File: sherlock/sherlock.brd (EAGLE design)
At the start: 91.4 x 58.4 mm, 27 parts, among them U3 XBEE-1B2, X1 2540-

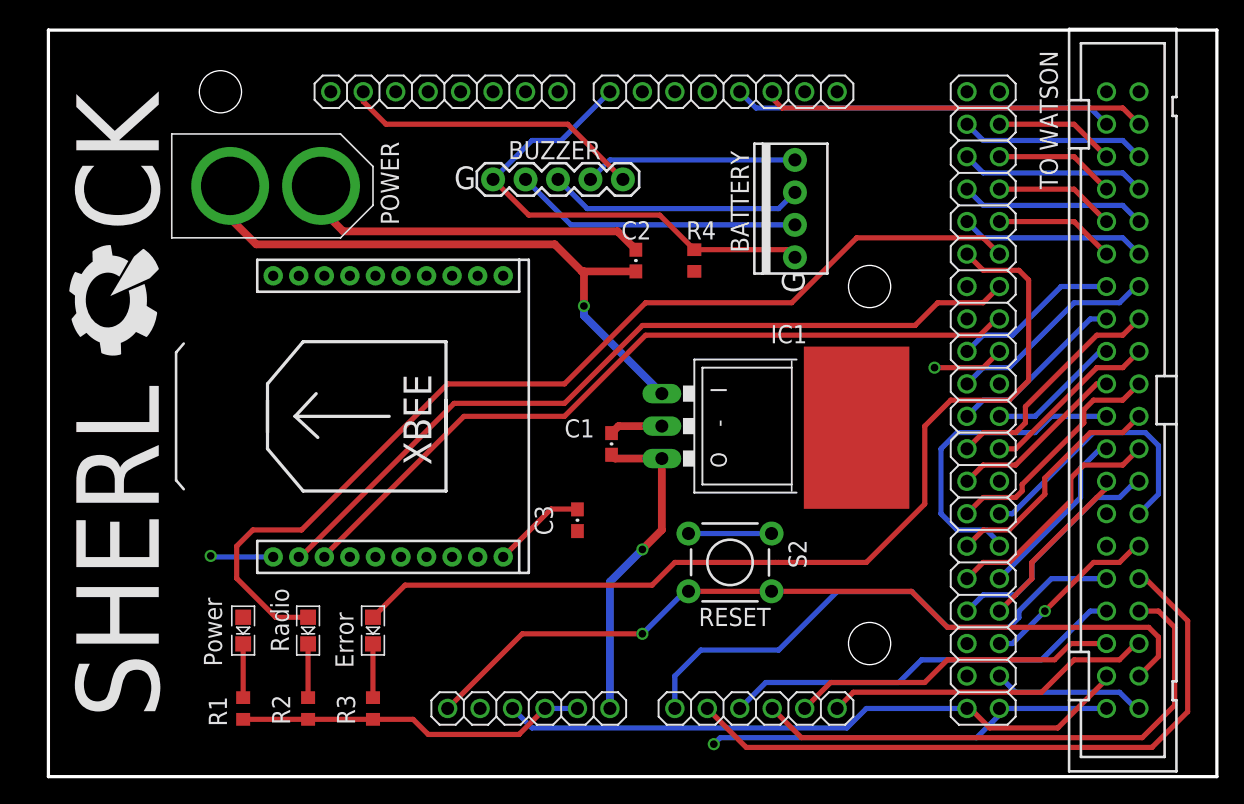
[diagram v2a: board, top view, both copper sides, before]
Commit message: Added Andersons
Also deleted sherlock_anderson because it's outdated and redundant (uses
last year's Sherlock).
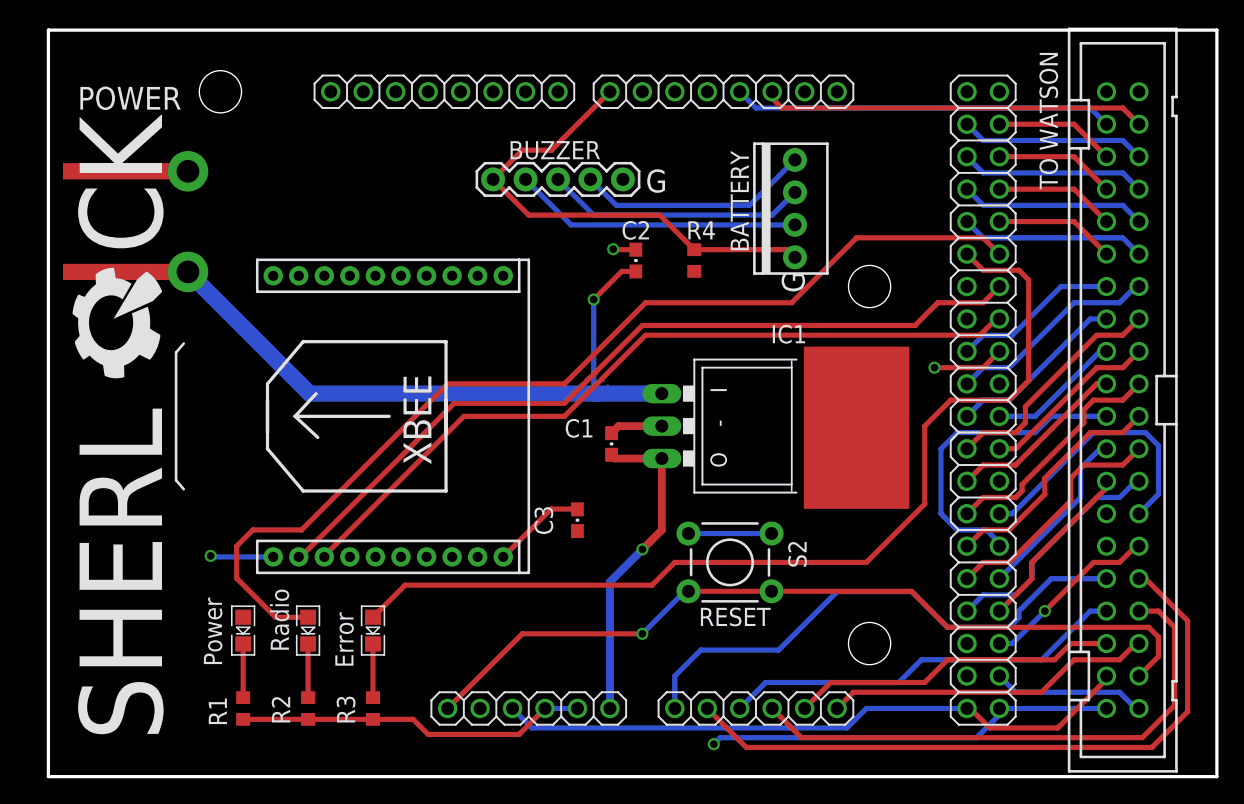
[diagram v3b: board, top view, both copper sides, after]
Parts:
- removed U$1: XT60CONNECTOR, pie:XT60CONNECTOR
- added POWER: ANDERSONHORIZONTAL, pie:ANDERSON_HORIZONTAL
- moved U$2 1.80 mm to (8.89, 2.79)
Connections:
- net 12V: now also POWER.PIN2; no longer U$1.12V
- net GND: now also POWER.PIN1; no longer U$1.GND
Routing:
- net GND: track 114.2 -> 64.7 mm, vias 1 -> 2
- net 12V: track 48.1 -> 52.7 mm
- net N$5: track 16.6 -> 18.3 mm
- added copper zone on layer 16, net 12V
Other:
- board text added: "2014.01.05"
- board text added: "Sherlock V2.0 Rev B"
- board text removed: "2013.10.13"
- board text removed: "POWER"
- board text removed: "Sherlock V2.0 Rev A"
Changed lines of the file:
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@@
 <layer number="97" name="Info" color="7" fill="1" visible="no" active="no"/>
 <layer number="98" name="Guide" color="6" fill="1" visible="no" active="no"/>
+<layer number="99" name="SpiceOrder" color="5" fill="1" visible="no" active="no"/>
 <layer number="100" name="ISO" color="7" fill="1" visible="yes" active="yes"/>
 <layer number="101" name="Design Layout" color="10" fill="1" visible="no" active="no"/>
@@
 <text x="43.053" y="17.907" size="1.016" layer="21" font="vector" rot="R180"></text>
 <text x="9.652" y="35.814" size="1.778" layer="22" font="vector" rot="MR180">Pioneers in Engineering</text>
-<text x="21.336" y="33.274" size="1.778" layer="22" font="vector" rot="MR180">2013.10.13</text>
-<text x="13.462" y="30.734" size="1.778" layer="22" font="vector" rot="MR180">Sherlock V2.0 Rev A</text>
-<text x="31.75" y="45.974" size="1.778" layer="21" font="vector">G</text>
+<text x="21.336" y="33.274" size="1.778" layer="22" font="vector" rot="MR180">2014.01.05</text>
+<text x="13.462" y="30.734" size="1.778" layer="22" font="vector" rot="MR180">Sherlock V2.0 Rev B</text>
+<text x="46.736" y="45.72" size="1.778" layer="21" font="vector">G</text>
 <text x="59.182" y="37.846" size="1.778" layer="21" font="vector" rot="R90">G</text>
-<text x="27.432" y="43.18" size="1.4224" layer="21" font="vector" ratio="15" rot="R90">POWER</text>
 <text x="78.994" y="45.974" size="1.4224" layer="21" font="vector" ratio="15" rot="R90">TO WATSON</text>
 <text x="45.72" y="8.89" size="1.27" layer="22" font="vector" ratio="15" rot="SMR0">Copyright (c) 2013,
@@
 <attribute name="PARTNUMBER" value="497-1446-5-ND" x="56.896" y="27.432" size="1.778" layer="27" rot="R270" display="off"/>
 </element>
-<element name="U$1" library="pie" package="XT60CONNECTOR" value="XT60CONNECTOR" x="17.78" y="46.228">
-<attribute name="PARTNUMBER" value="PRT-10474 " x="17.78" y="46.228" size="1.778" layer="27" display="off"/>
-</element>
 <element name="BATTERY" library="pie" package="1X04-MTA" value="" x="58.42" y="44.45" smashed="yes" rot="R90">
 <attribute name="NAME" x="53.3908" y="48.9712" size="1.4224" layer="25" font="vector" ratio="15" rot="R270"/>
@@
 </element>
 <element name="U$7" library="pie" package="OSHW-LOGO-L" value="" x="60.198" y="28.448" rot="MR0"/>
-<element name="U$2" library="pie" package="SHERLOCK" value="" x="8.636" y="4.572" rot="R90"/>
+<element name="U$2" library="pie" package="SHERLOCK" value="" x="8.89" y="2.794" smashed="yes" rot="R90"/>
+<element name="POWER" library="pie" package="ANDERSON_HORIZONTAL" value="ANDERSONHORIZONTAL" x="10.922" y="43.434" smashed="yes">
+<attribute name="PARTNUMBER" value="1377G1" x="10.922" y="43.434" size="1.778" layer="27" display="off"/>
+<attribute name="NAME" x="2.286" y="52.197" size="1.778" layer="25" font="vector"/>
+</element>
 </elements>
 <signals>
@@
 <via x="69.342" y="32.004" extent="1-16" drill="0.6"/>
 <contactref element="C2" pad="2"/>
-<polygon width="0.6096" layer="16" isolate="0.2794">
+<polygon width="0.6096" layer="16" isolate="0.2794" rank="2">
 <vertex x="0" y="0"/>
 <vertex x="91.44" y="0"/>
@@
 <vertex x="0" y="58.42"/>
 </polygon>
-<wire x1="44.538" y1="42.672" x2="23.07" y2="42.672" width="0.6096" layer="1"/>
 <wire x1="44.069" y1="26.885" x2="44.616" y2="27.432" width="0.6096" layer="1"/>
 <wire x1="44.616" y1="27.432" x2="48.006" y2="27.432" width="0.6096" layer="1"/>
@@
 <wire x1="25.4" y1="4.484" x2="20.32" y2="4.484" width="0.4064" layer="1"/>
 <wire x1="20.32" y1="4.484" x2="15.24" y2="4.484" width="0.4064" layer="1"/>
-<wire x1="44.538" y1="42.672" x2="45.974" y2="41.236" width="0.6096" layer="1"/>
 <wire x1="41.377" y1="20.941" x2="41.402" y2="20.916" width="0.4064" layer="1"/>
 <wire x1="28.536" y1="4.484" x2="29.718" y2="3.302" width="0.4064" layer="1"/>
@@
 <contactref element="S2" pad="3"/>
 <wire x1="50.0888" y1="19.0246" x2="56.5912" y2="19.0246" width="0.4064" layer="16"/>
-<contactref element="U$1" pad="GND"/>
-<wire x1="23.07" y1="42.672" x2="21.336" y2="44.406" width="0.6096" layer="1"/>
-<wire x1="21.336" y1="44.406" x2="21.336" y2="46.228" width="0.6096" layer="1"/>
 <wire x1="28.536" y1="4.484" x2="25.4" y2="4.484" width="0.4064" layer="1"/>
 <contactref element="BUZZER" pad="5"/>
-<wire x1="44.958" y1="46.736" x2="40.64" y2="51.054" width="0.4064" layer="1"/>
-<wire x1="40.64" y1="51.054" x2="26.416" y2="51.054" width="0.4064" layer="1"/>
-<wire x1="26.416" y1="51.054" x2="24.638" y2="52.832" width="0.4064" layer="1"/>
-<wire x1="24.638" y1="52.832" x2="24.638" y2="53.594" width="0.4064" layer="1"/>
+<contactref element="POWER" pad="PIN1"/>
+<wire x1="43.815" y1="41.275" x2="43.815" y2="41.275" width="0" layer="19" extent="1-16"/>
+<wire x1="45.974" y1="41.236" x2="44.235" y2="41.236" width="0.4064" layer="1"/>
+<wire x1="44.235" y1="41.236" x2="44.196" y2="41.275" width="0.4064" layer="1"/>
+<via x="44.196" y="41.275" extent="1-16" drill="0.6"/>
+<wire x1="44.196" y1="41.275" x2="42.799" y2="41.275" width="0" layer="19" extent="1-16"/>
+<wire x1="42.799" y1="41.275" x2="41.91" y2="42.164" width="0" layer="19" extent="1-16"/>
+<wire x1="41.91" y1="42.164" x2="44.958" y2="46.736" width="0" layer="19" extent="1-16"/>
 </signal>
 <signal name="VCC" class="1">
@@
 <contactref element="BUZZER" pad="1"/>
 <contactref element="R4" pad="2"/>
-<wire x1="43.942" y1="53.594" x2="40.132" y2="49.784" width="0.4064" layer="16"/>
-<wire x1="40.132" y1="49.784" x2="37.846" y2="49.784" width="0.4064" layer="16"/>
-<wire x1="34.798" y1="46.736" x2="37.846" y2="49.784" width="0.4064" layer="16"/>
 <wire x1="47.84" y1="43.942" x2="37.592" y2="43.942" width="0.4064" layer="1"/>
 <wire x1="37.592" y1="43.942" x2="34.798" y2="46.736" width="0.4064" layer="1"/>
@@
 <wire x1="58.42" y1="40.64" x2="57.824" y2="41.236" width="0.4064" layer="1"/>
 <wire x1="57.824" y1="41.236" x2="50.546" y2="41.236" width="0.4064" layer="1"/>
+<wire x1="34.798" y1="46.736" x2="37.084" y2="49.022" width="0.4064" layer="1"/>
+<wire x1="37.084" y1="49.022" x2="39.37" y2="49.022" width="0.4064" layer="1"/>
+<wire x1="39.37" y1="49.022" x2="43.942" y2="53.594" width="0.4064" layer="1"/>
 </signal>
 <signal name="MOSI0/IO41*">
@@
 <signal name="12V">
 <contactref element="IC1" pad="IN"/>
-<contactref element="U$1" pad="12V"/>
 <contactref element="C2" pad="1"/>
-<wire x1="14.224" y1="46.228" x2="14.224" y2="43.688" width="0.6096" layer="1"/>
-<wire x1="14.224" y1="43.688" x2="16.256" y2="41.656" width="0.6096" layer="1"/>
-<wire x1="39.624" y1="41.656" x2="16.256" y2="41.656" width="0.6096" layer="1"/>
-<via x="41.91" y="36.83" extent="1-16" drill="0.6"/>
-<wire x1="41.91" y1="36.83" x2="41.91" y2="39.536" width="0.6096" layer="1"/>
-<wire x1="48.006" y1="29.972" x2="41.91" y2="36.068" width="0.6096" layer="16"/>
-<wire x1="41.91" y1="36.068" x2="41.91" y2="36.83" width="0.6096" layer="16"/>
-<wire x1="39.624" y1="41.656" x2="41.744" y2="39.536" width="0.6096" layer="1"/>
-<wire x1="41.744" y1="39.536" x2="41.91" y2="39.536" width="0.6096" layer="1"/>
-<wire x1="41.91" y1="39.536" x2="45.974" y2="39.536" width="0.6096" layer="1"/>
+<contactref element="POWER" pad="PIN2"/>
+<wire x1="48.006" y1="29.972" x2="42.926" y2="29.972" width="1.27" layer="16"/>
+<wire x1="42.926" y1="29.972" x2="20.447" y2="29.972" width="1.27" layer="16"/>
+<wire x1="20.447" y1="29.972" x2="10.922" y2="39.497" width="1.27" layer="16"/>
+<via x="42.672" y="37.338" extent="1-16" drill="0.6"/>
+<wire x1="42.672" y1="37.338" x2="42.672" y2="30.226" width="0.4064" layer="16"/>
+<wire x1="42.672" y1="30.226" x2="42.926" y2="29.972" width="0.4064" layer="16"/>
+<polygon width="0.4064" layer="16">
+<vertex x="41.402" y="30.48"/>
+<vertex x="42.672" y="31.75"/>
+<vertex x="43.942" y="30.48"/>
+</polygon>
+<wire x1="45.974" y1="39.536" x2="44.87" y2="39.536" width="0.4064" layer="1"/>
+<wire x1="44.87" y1="39.536" x2="42.672" y2="37.338" width="0.4064" layer="1"/>
 </signal>
 <signal name="SDA0/IO33*">
@@
 <contactref element="BATTERY" pad="4"/>
 <contactref element="BUZZER" pad="4"/>
-<wire x1="42.418" y1="46.736" x2="43.942" y2="48.26" width="0.4064" layer="16"/>
-<wire x1="43.942" y1="48.26" x2="58.42" y2="48.26" width="0.4064" layer="16"/>
+<wire x1="58.42" y1="48.26" x2="55.499" y2="45.339" width="0.4064" layer="16"/>
+<wire x1="55.499" y1="45.339" x2="55.372" y2="45.212" width="0.4064" layer="16"/>
+<wire x1="44.45" y1="44.704" x2="42.418" y2="46.736" width="0.4064" layer="16"/>
+<wire x1="44.45" y1="44.704" x2="54.864" y2="44.704" width="0.4064" layer="16"/>
+<wire x1="54.864" y1="44.704" x2="55.372" y2="45.212" width="0.4064" layer="16"/>
 </signal>
 <signal name="N$6">
 <contactref element="BUZZER" pad="3"/>
 <contactref element="BATTERY" pad="3"/>
-<wire x1="39.878" y1="46.736" x2="42.164" y2="44.45" width="0.4064" layer="16"/>
-<wire x1="42.164" y1="44.45" x2="57.15" y2="44.45" width="0.4064" layer="16"/>
-<wire x1="57.15" y1="44.45" x2="58.42" y2="45.72" width="0.4064" layer="16"/>
+<wire x1="39.878" y1="46.736" x2="42.672" y2="43.942" width="0.4064" layer="16"/>
+<wire x1="56.642" y1="43.942" x2="58.42" y2="45.72" width="0.4064" layer="16"/>
+<wire x1="42.672" y1="43.942" x2="56.642" y2="43.942" width="0.4064" layer="16"/>
 </signal>
 <signal name="N$7">

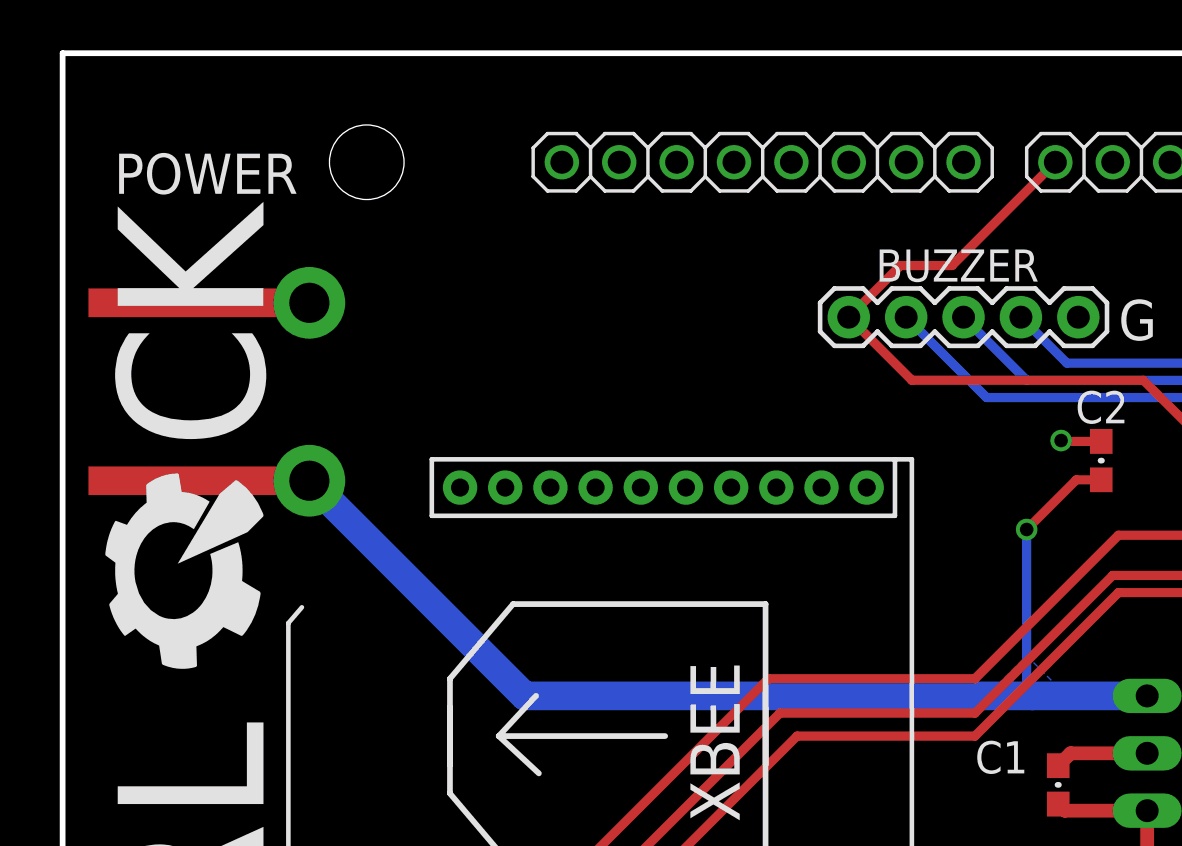
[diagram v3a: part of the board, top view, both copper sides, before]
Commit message: Fixed schematics and added labels
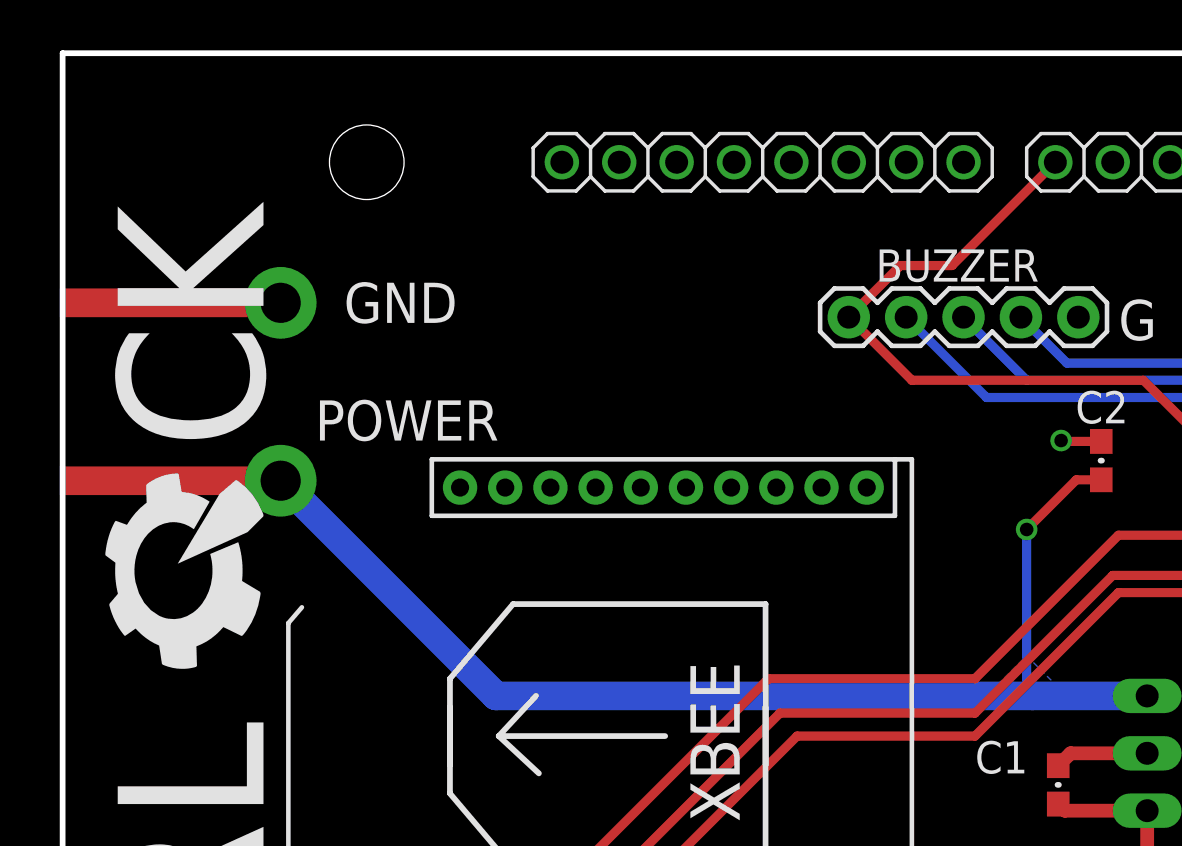
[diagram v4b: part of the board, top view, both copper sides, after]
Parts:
- moved POWER 1.27 mm to (9.65, 43.4)
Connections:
- net N$5 renamed CELL_3
- net N$6 renamed CELL_2
- net N$7 renamed CELL_1
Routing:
- net 12V: track 52.7 -> 54.0 mm
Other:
- board text added: "GND"
- board text added: "Sherlock V2.0 Rev C"
- board text removed: "Sherlock V2.0 Rev B"
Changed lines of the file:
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@@
 <text x="9.652" y="35.814" size="1.778" layer="22" font="vector" rot="MR180">Pioneers in Engineering</text>
 <text x="21.336" y="33.274" size="1.778" layer="22" font="vector" rot="MR180">2014.01.05</text>
-<text x="13.462" y="30.734" size="1.778" layer="22" font="vector" rot="MR180">Sherlock V2.0 Rev B</text>
+<text x="13.462" y="30.734" size="1.778" layer="22" font="vector" rot="MR180">Sherlock V2.0 Rev C</text>
 <text x="46.736" y="45.72" size="1.778" layer="21" font="vector">G</text>
 <text x="59.182" y="37.846" size="1.778" layer="21" font="vector" rot="R90">G</text>
@@
 For more information, visit
 pioneers.berkeley.edu/opensource</text>
+<text x="12.446" y="46.482" size="1.778" layer="21" font="vector">GND</text>
 </plain>
 <attributes>
@@
 <element name="U$7" library="pie" package="OSHW-LOGO-L" value="" x="60.198" y="28.448" rot="MR0"/>
 <element name="U$2" library="pie" package="SHERLOCK" value="" x="8.89" y="2.794" smashed="yes" rot="R90"/>
-<element name="POWER" library="pie" package="ANDERSON_HORIZONTAL" value="ANDERSONHORIZONTAL" x="10.922" y="43.434" smashed="yes">
-<attribute name="PARTNUMBER" value="1377G1" x="10.922" y="43.434" size="1.778" layer="27" display="off"/>
-<attribute name="NAME" x="2.286" y="52.197" size="1.778" layer="25" font="vector"/>
+<element name="POWER" library="pie" package="ANDERSON_HORIZONTAL" value="ANDERSONHORIZONTAL" x="9.652" y="43.434" smashed="yes">
+<attribute name="PARTNUMBER" value="1377G1" x="9.652" y="43.434" size="1.778" layer="27" display="off"/>
+<attribute name="NAME" x="11.176" y="41.275" size="1.778" layer="25" font="vector"/>
 </element>
 </elements>
@@
 <contactref element="POWER" pad="PIN2"/>
 <wire x1="48.006" y1="29.972" x2="42.926" y2="29.972" width="1.27" layer="16"/>
-<wire x1="42.926" y1="29.972" x2="20.447" y2="29.972" width="1.27" layer="16"/>
-<wire x1="20.447" y1="29.972" x2="10.922" y2="39.497" width="1.27" layer="16"/>
+<wire x1="42.926" y1="29.972" x2="19.177" y2="29.972" width="1.27" layer="16"/>
 <via x="42.672" y="37.338" extent="1-16" drill="0.6"/>
 <wire x1="42.672" y1="37.338" x2="42.672" y2="30.226" width="0.4064" layer="16"/>
@@
 <wire x1="45.974" y1="39.536" x2="44.87" y2="39.536" width="0.4064" layer="1"/>
 <wire x1="44.87" y1="39.536" x2="42.672" y2="37.338" width="0.4064" layer="1"/>
+<wire x1="19.177" y1="29.972" x2="9.652" y2="39.497" width="1.27" layer="16"/>
 </signal>
 <signal name="SDA0/IO33*">
@@
 <contactref element="P2" pad="1"/>
 </signal>
-<signal name="N$5">
+<signal name="CELL_3">
 <contactref element="BATTERY" pad="4"/>
 <contactref element="BUZZER" pad="4"/>
@@
 <wire x1="54.864" y1="44.704" x2="55.372" y2="45.212" width="0.4064" layer="16"/>
 </signal>
-<signal name="N$6">
+<signal name="CELL_2">
 <contactref element="BUZZER" pad="3"/>
 <contactref element="BATTERY" pad="3"/>
@@
 <wire x1="42.672" y1="43.942" x2="56.642" y2="43.942" width="0.4064" layer="16"/>
 </signal>
-<signal name="N$7">
+<signal name="CELL_1">
 <contactref element="BATTERY" pad="2"/>
 <contactref element="BUZZER" pad="2"/>
